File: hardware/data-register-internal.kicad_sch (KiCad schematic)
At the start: 4 parts, among them U14 74LV164D,118, U15 74LV164D,118

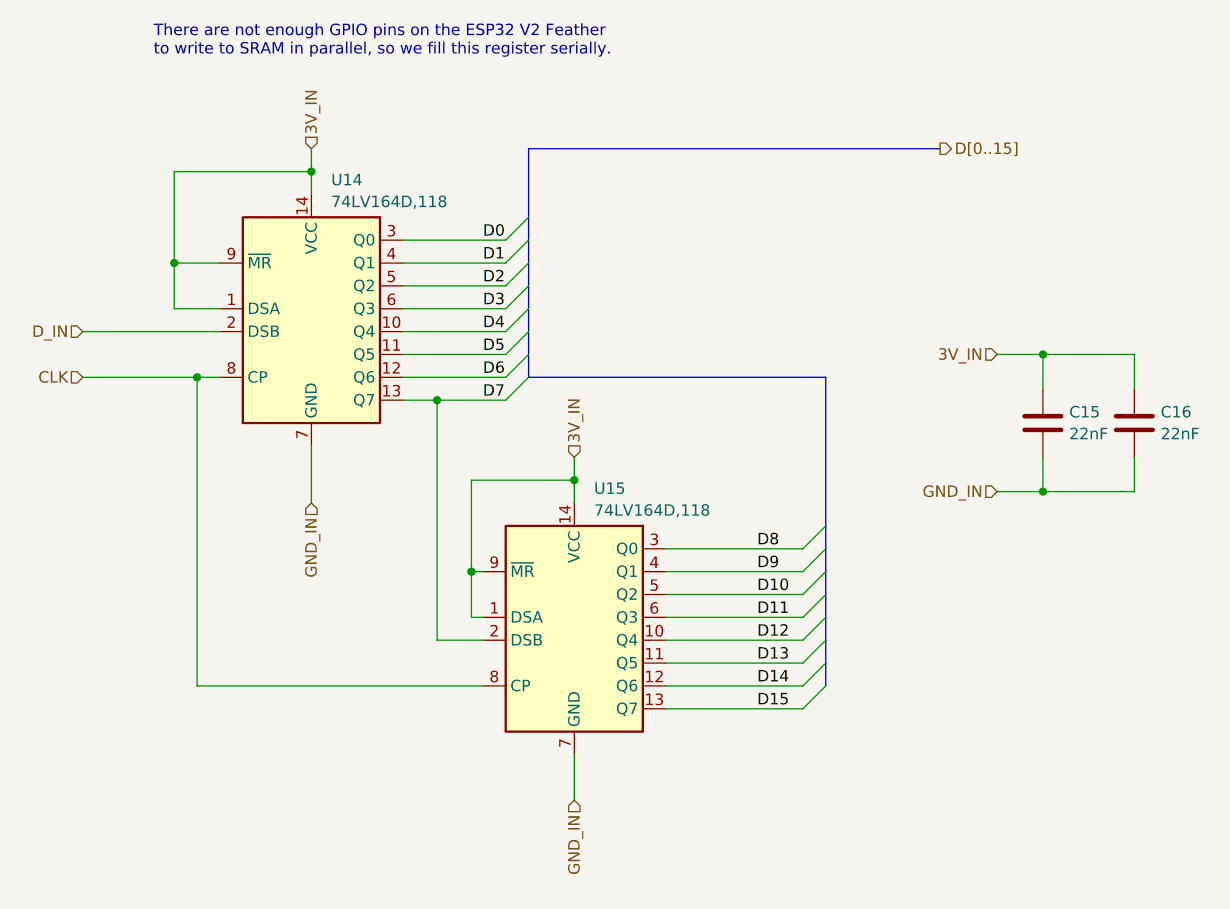
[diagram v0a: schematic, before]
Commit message: Massively reorganize board designs
Now planning to have most assembly done by JLCPCB, so trace sizes,
part selections, etc. are set accordingly.

New boards are:
 - cartridge interface & flash
 - microcontroller & registers
 - sram x2
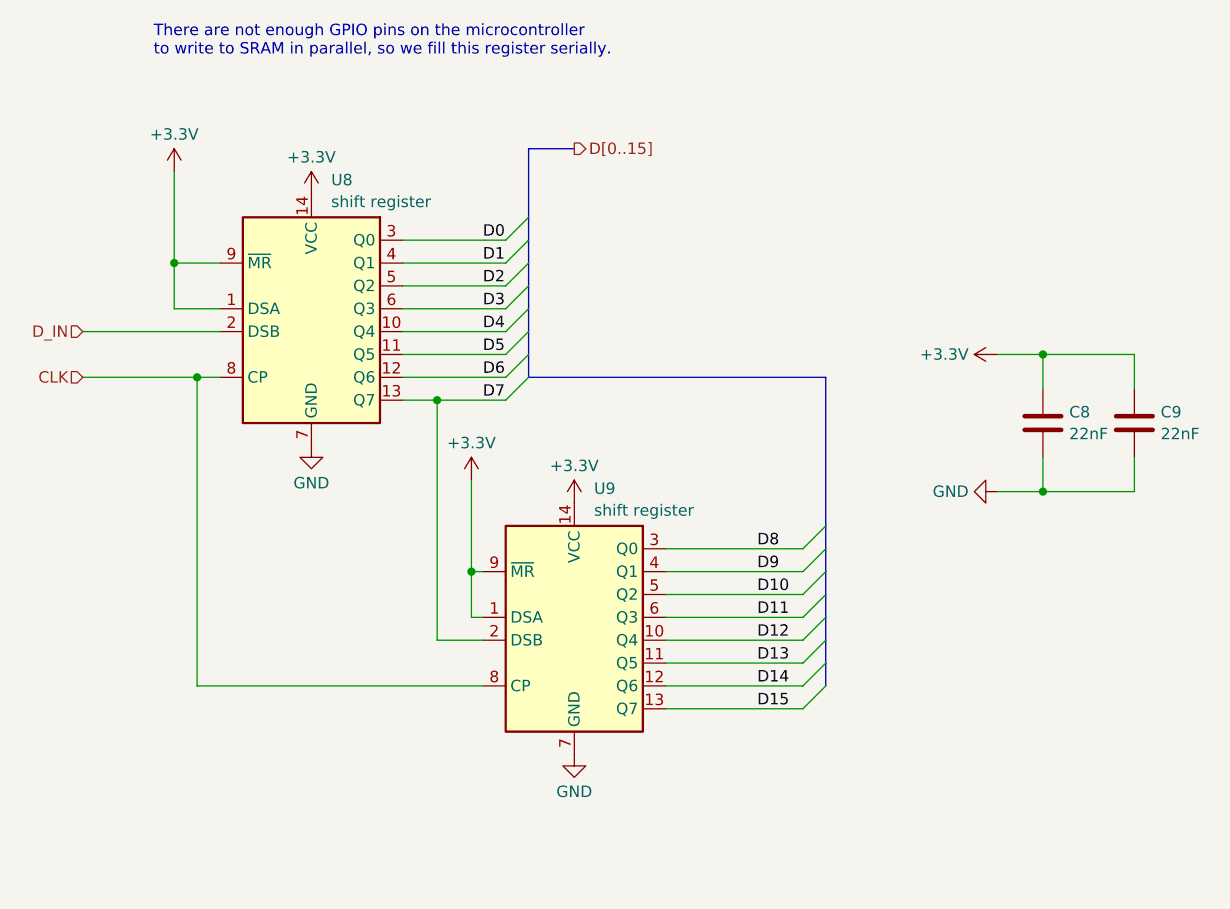
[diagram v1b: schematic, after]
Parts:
- C8: renamed from C15; JLCPCB Part Number (none) -> C21122; Mouser Part Number (none) -> 187-CL10B223KB8NNNC; Part Number (none) -> CL10B223KB8NNNC
- C9: renamed from C16; JLCPCB Part Number (none) -> C21122; Mouser Part Number (none) -> 187-CL10B223KB8NNNC; Part Number (none) -> CL10B223KB8NNNC
- U8: renamed from U14; value 74LV164D,118 -> shift register; footprint Package_SO:SOIC-14_3.9x8.7mm_P1.27mm -> Package_SO:TSSOP-14_4.4x5mm_P0.65mm; JLCPCB Part Number (none) -> C179331; Mouser Part Number (none) -> 771-LV164PW118; Part Number (none) -> 74LV164PW,118
- U9: renamed from U15; value 74LV164D,118 -> shift register; footprint Package_SO:SOIC-14_3.9x8.7mm_P1.27mm -> Package_SO:TSSOP-14_4.4x5mm_P0.65mm; JLCPCB Part Number (none) -> C179331; Mouser Part Number (none) -> 771-LV164PW118; Part Number (none) -> 74LV164PW,118
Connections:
- net 3V_IN renamed +3.3V
- net GND_IN renamed GND
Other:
- note added: "There are not enough GPIO pins on the microcontroller to write to SRAM in parallel, so we fill this register serially."
- note removed: "There are not enough GPIO pins on the ESP32 V2 Feather to write to SRAM in parallel, so we fill this register serially."

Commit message: Revise microcontroller board based on latest cart board improvements
 - Update comments
 - Segregate the Ethernet module's power supply so it can be
   disconnected if something goes wrong in a prototype
 - Update board setup to match latest cart board
 - Remove unnecessary level-shifter
 - Fix address decoder to non-latching version
 - Fix address decoder output assignment
 - Consolidate buffer ICs in register file
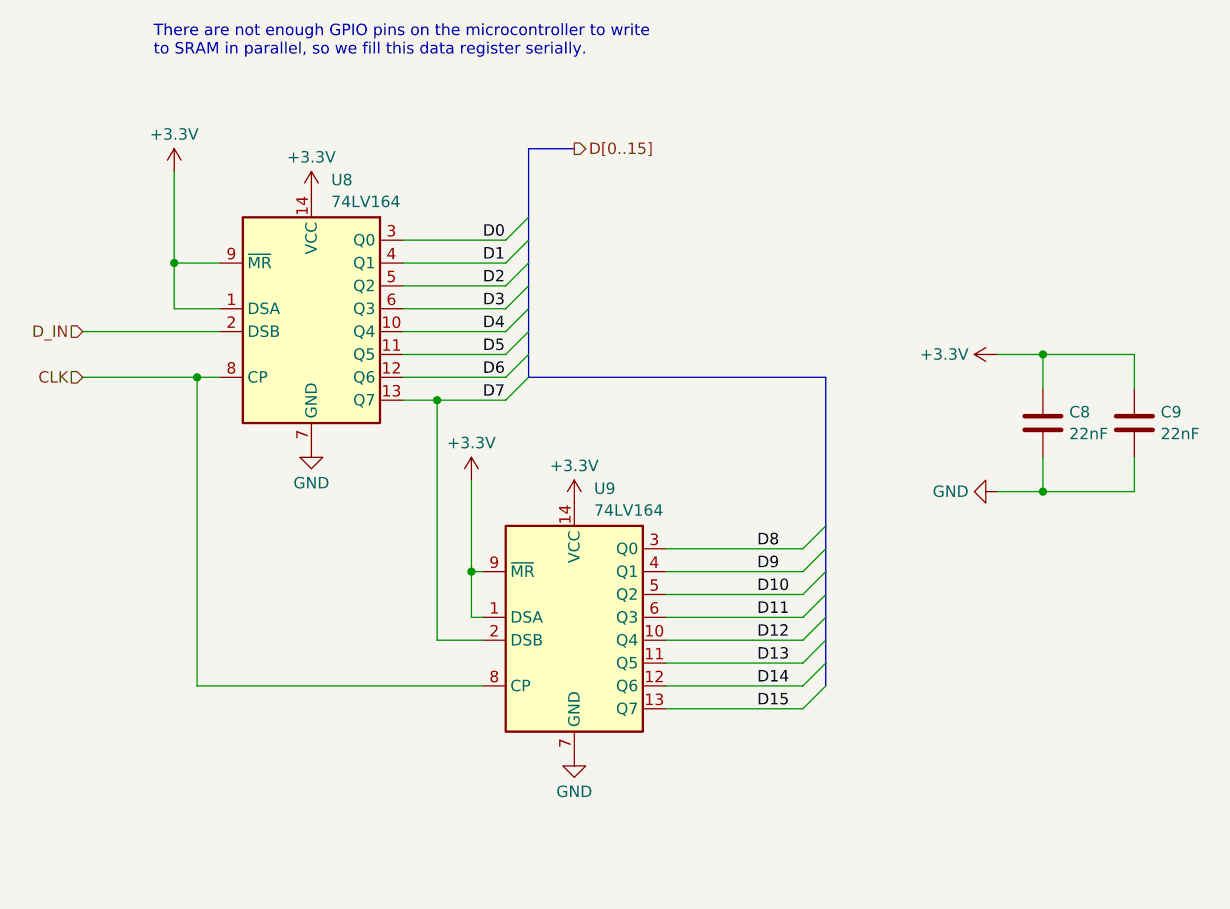
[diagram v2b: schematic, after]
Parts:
- U8, U9: value shift register -> 74LV164
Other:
- note added: "There are not enough GPIO pins on the microcontroller to write to SRAM in parallel, so we fill this data register serially."
- note removed: "There are not enough GPIO pins on the microcontroller to write to SRAM in parallel, so we fill this register serially."
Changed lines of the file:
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@@
 		)
 	)
-	(text "There are not enough GPIO pins on the microcontroller\nto write to SRAM in parallel, so we fill this register serially."
+	(text "There are not enough GPIO pins on the microcontroller to write\nto SRAM in parallel, so we fill this data register serially."
 		(exclude_from_sim no)
 		(at 38.354 31.242 0)
@@
 			)
 		)
-		(property "Value" "shift register"
+		(property "Value" "74LV164"
 			(at 58.0741 49.0798 0)
 			(effects
@@
 			)
 		)
-		(property "Value" "shift register"
+		(property "Value" "74LV164"
 			(at 87.2841 83.3698 0)
 			(effects

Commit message: Improve uC board assembly process, fix minor bug
Changes to part numbers to better align with JLCPCB stock:
 - Replace 74LV164PW,118 / C179331 with SN74LV164APWR / C403720
 - Replace SN74LV163APWR / C2675453 with SN74LV161APWR / C2649404
   - Original had sync clear, but this is async clear, which is a bug
     fix!
 - Fix rotation of U8, U9, U13
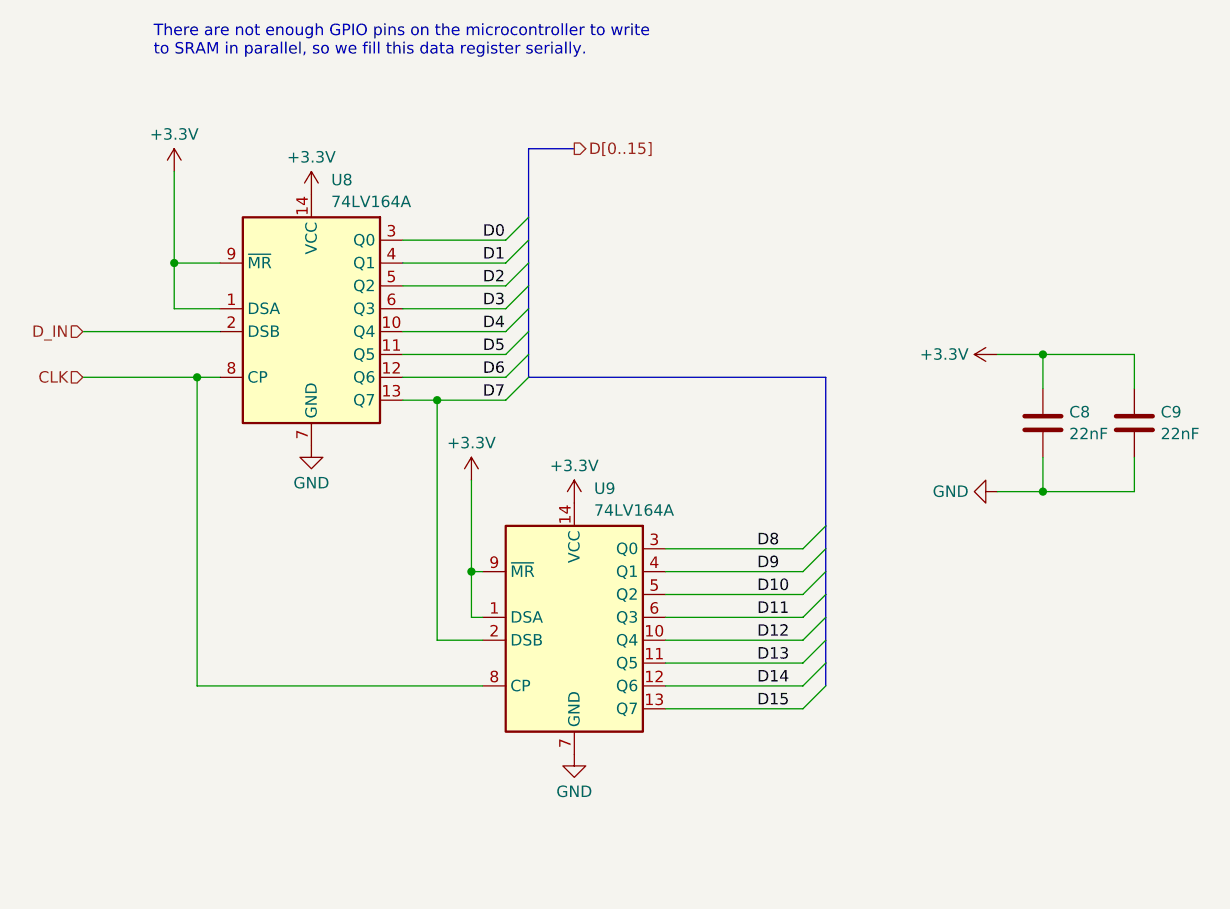
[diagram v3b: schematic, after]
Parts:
- U8, U9: value 74LV164 -> 74LV164A; JLCPCB Part Number C179331 -> C403720; Mouser Part Number 771-LV164PW118 -> 595-SN74LV164APWR; Part Number 74LV164PW,118 -> SN74LV164APWR
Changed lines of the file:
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@@
 			)
 		)
-		(property "Value" "74LV164"
+		(property "Value" "74LV164A"
 			(at 58.0741 49.0798 0)
 			(effects
@@
 			)
 		)
-		(property "Datasheet" "https://www.mouser.com/datasheet/2/916/74LV164-1517637.pdf"
+		(property "Datasheet" "https://www.ti.com/lit/gpn/sn74lv164a"
 			(at 78.74 68.58 0)
 			(effects
@@
 			)
 		)
-		(property "Mouser Part Number" "771-LV164PW118"
+		(property "Mouser Part Number" "595-SN74LV164APWR"
 			(at 55.88 60.96 0)
 			(effects
@@
 			)
 		)
-		(property "Part Number" "74LV164PW,118"
+		(property "Part Number" "SN74LV164APWR"
 			(at 55.88 60.96 0)
 			(effects
@@
 			)
 		)
-		(property "JLCPCB Part Number" "C179331"
+		(property "JLCPCB Part Number" "C403720"
 			(at 55.88 60.96 0)
 			(effects
@@
 			)
 		)
-		(property "Value" "74LV164"
+		(property "Value" "74LV164A"
 			(at 87.2841 83.3698 0)
 			(effects
@@
 			)
 		)
-		(property "Datasheet" "https://www.mouser.com/datasheet/2/916/74LV164-1517637.pdf"
+		(property "Datasheet" "https://www.ti.com/lit/gpn/sn74lv164a"
 			(at 107.95 102.87 0)
 			(effects
@@
 			)
 		)
-		(property "Mouser Part Number" "771-LV164PW118"
+		(property "Mouser Part Number" "595-SN74LV164APWR"
 			(at 85.09 95.25 0)
 			(effects
@@
 			)
 		)
-		(property "Part Number" "74LV164PW,118"
+		(property "Part Number" "SN74LV164APWR"
 			(at 85.09 95.25 0)
 			(effects
@@
 			)
 		)
-		(property "JLCPCB Part Number" "C179331"
+		(property "JLCPCB Part Number" "C403720"
 			(at 85.09 95.25 0)
 			(effects
